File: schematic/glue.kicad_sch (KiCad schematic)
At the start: 9 parts, among them J6 Conn_02x05_Odd_Even, U9 EPM7128SLC

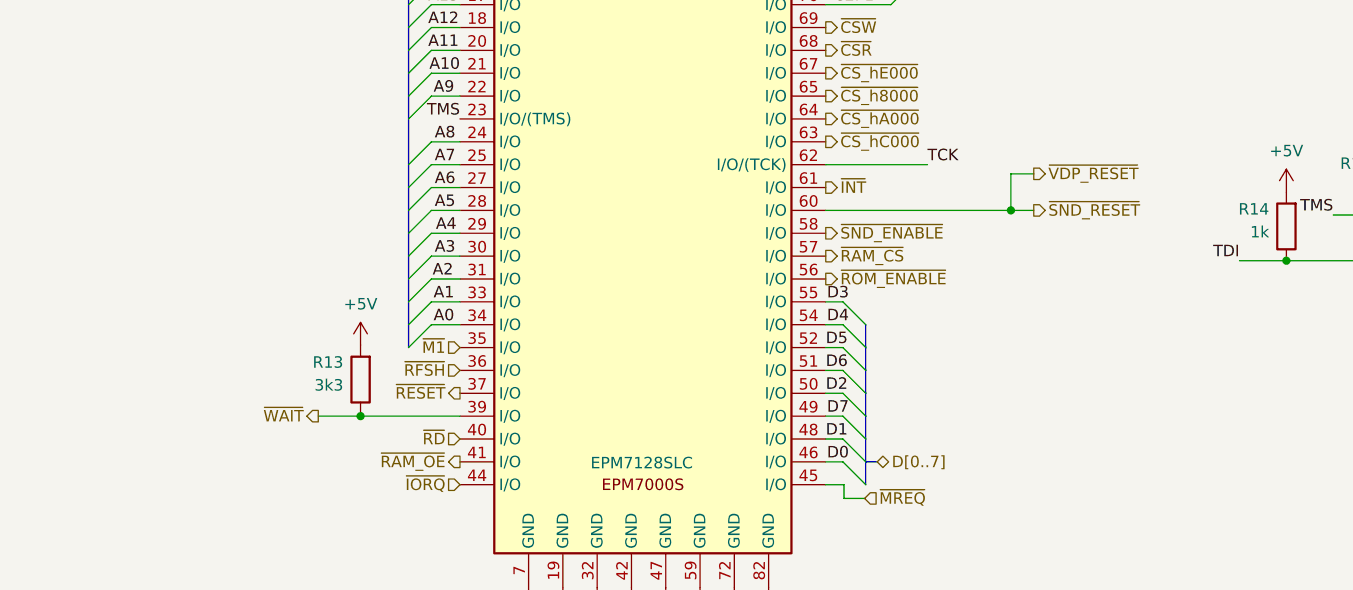
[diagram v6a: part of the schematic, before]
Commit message: complete ram mirror when banks not enabled.
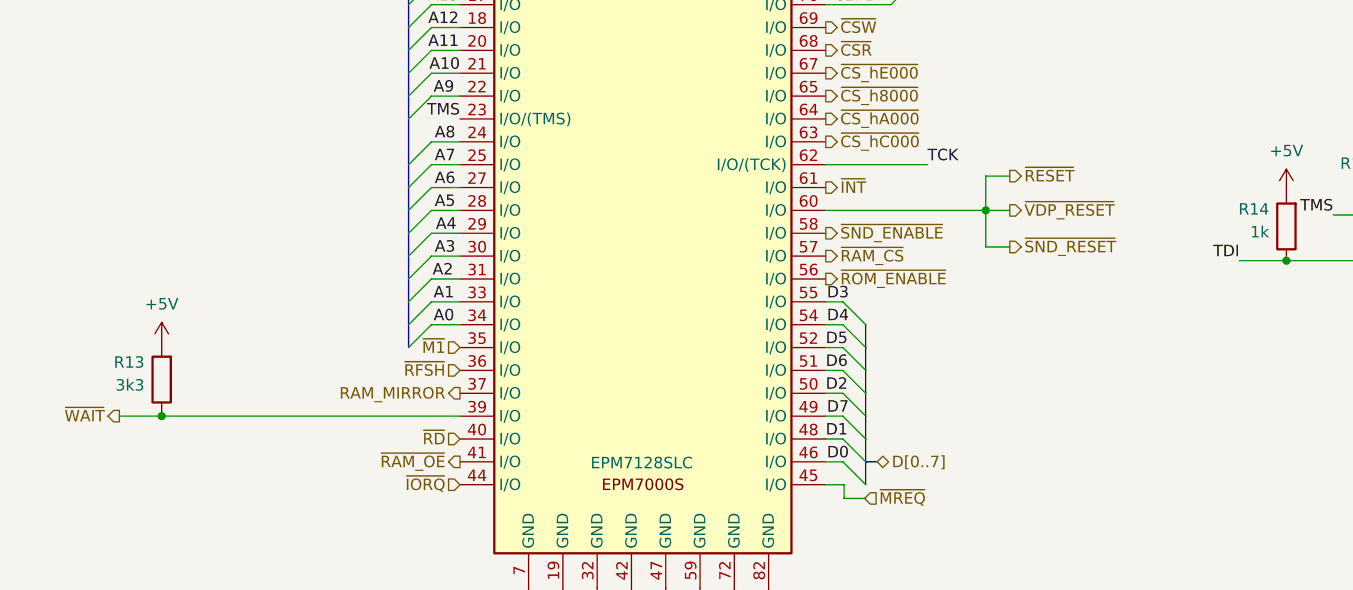
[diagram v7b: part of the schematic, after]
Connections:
- net ~{SND_RESET} is gone; now on net ~{RESET}: U9.60 (I/O)
- net ~{RESET}: no longer U9.37 (I/O)
- new net RAM_MIRROR: U9.37 (I/O)
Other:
- moved on the sheet: R13
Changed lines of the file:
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@@
   (junction (at 184.531 114.3) (diameter 0) (color 0 0 0 0)
   )
-  (junction (at 70.358 136.652) (diameter 0) (color 0 0 0 0)
+  (junction (at 48.26 136.652) (diameter 0) (color 0 0 0 0)
   )
   (junction (at 142.367 48.641) (diameter 0) (color 0 0 0 0)
@@
   (junction (at 142.367 40.386) (diameter 0) (color 0 0 0 0)
   )
-  (junction (at 142.621 113.792) (diameter 0) (color 0 0 0 0)
+  (junction (at 139.827 113.792) (diameter 0) (color 0 0 0 0)
   )
   (no_connect (at 225.298 114.3))
@@
     (stroke (width 0) (type default))
   )
-  (wire (pts (xy 145.161 113.792) (xy 142.621 113.792))
+  (wire (pts (xy 142.494 113.792) (xy 139.827 113.792))
     (stroke (width 0) (type default))
   )
@@
     (stroke (width 0) (type default))
   )
-  (wire (pts (xy 142.494 113.792) (xy 122.047 113.792))
-    (stroke (width 0) (type default))
-  )
   (bus (pts (xy 69.596 62.865) (xy 71.12 62.865))
     (stroke (width 0) (type default))
@@
     (stroke (width 0) (type default))
   )
-  (wire (pts (xy 70.358 136.652) (xy 70.358 136.398))
+  (wire (pts (xy 48.26 136.652) (xy 48.26 136.398))
     (stroke (width 0) (type default))
   )
@@
     (stroke (width 0) (type default))
   )
-  (wire (pts (xy 142.621 113.792) (xy 142.621 113.919))
-    (stroke (width 0) (type default))
-  )
   (bus (pts (xy 75.692 111.252) (xy 75.692 113.792))
     (stroke (width 0) (type default))
@@
     (stroke (width 0) (type default))
   )
-  (wire (pts (xy 145.161 109.728) (xy 142.621 109.728))
-    (stroke (width 0) (type default))
-  )
   (wire (pts (xy 78.232 123.952) (xy 81.407 123.952))
     (stroke (width 0) (type default))
@@
     (stroke (width 0) (type default))
   )
+  (wire (pts (xy 139.827 117.856) (xy 142.494 117.856))
+    (stroke (width 0) (type default))
+  )
   (bus (pts (xy 75.692 126.492) (xy 75.692 129.032))
     (stroke (width 0) (type default))
@@
     (stroke (width 0) (type default))
   )
-  (wire (pts (xy 65.659 136.652) (xy 70.358 136.652))
+  (wire (pts (xy 43.561 136.652) (xy 48.26 136.652))
     (stroke (width 0) (type default))
   )
@@
     (stroke (width 0) (type default))
   )
+  (wire (pts (xy 142.494 109.982) (xy 139.827 109.982))
+    (stroke (width 0) (type default))
+  )
   (wire (pts (xy 122.047 80.772) (xy 129.286 80.772))
     (stroke (width 0) (type default))
@@
     (stroke (width 0) (type default))
   )
-  (wire (pts (xy 142.494 113.919) (xy 142.494 113.792))
-    (stroke (width 0) (type default))
-  )
   (wire (pts (xy 122.047 83.312) (xy 129.286 83.312))
     (stroke (width 0) (type default))
@@
     (stroke (width 0) (type default))
   )
-  (wire (pts (xy 70.358 136.652) (xy 81.407 136.652))
+  (wire (pts (xy 48.26 136.652) (xy 81.407 136.652))
     (stroke (width 0) (type default))
   )
@@
     (stroke (width 0) (type default))
   )
+  (wire (pts (xy 139.827 113.792) (xy 139.827 117.856))
+    (stroke (width 0) (type default))
+  )
   (bus (pts (xy 75.692 118.872) (xy 75.692 121.412))
     (stroke (width 0) (type default))
@@
     (stroke (width 0) (type default))
   )
+  (wire (pts (xy 139.827 113.792) (xy 139.827 109.982))
+    (stroke (width 0) (type default))
+  )
   (wire (pts (xy 73.66 65.532) (xy 81.407 65.532))
     (stroke (width 0) (type default))
@@
     (stroke (width 0) (type default))
   )
+  (wire (pts (xy 122.047 113.792) (xy 139.827 113.792))
+    (stroke (width 0) (type default))
+  )
   (wire (pts (xy 81.407 90.932) (xy 78.232 90.932))
     (stroke (width 0) (type default))
@@
     (stroke (width 0) (type default))
   )
-  (wire (pts (xy 142.621 109.728) (xy 142.621 113.792))
-    (stroke (width 0) (type default))
-  )
-  (wire (pts (xy 142.621 113.919) (xy 142.494 113.919))
-    (stroke (width 0) (type default))
-  )
   (bus (pts (xy 131.826 83.312) (xy 131.826 86.36))
     (stroke (width 0) (type default))
@@
     (effects (font (size 1.27 1.27)) (justify left))
   )
+  (hierarchical_label "RAM_MIRROR" (shape output) (at 81.407 134.112 180) (fields_autoplaced)
+    (effects (font (size 1.27 1.27)) (justify right))
+  )
   (hierarchical_label "~{CSR}" (shape output) (at 122.047 96.012 0) (fields_autoplaced)
     (effects (font (size 1.27 1.27)) (justify left))
@@
     (effects (font (size 1.27 1.27)) (justify right))
   )
-  (hierarchical_label "~{WAIT}" (shape output) (at 65.659 136.652 180) (fields_autoplaced)
+  (hierarchical_label "~{WAIT}" (shape output) (at 43.561 136.652 180) (fields_autoplaced)
     (effects (font (size 1.27 1.27)) (justify right))
   )
@@
     (effects (font (size 1.27 1.27)) (justify left))
   )
-  (hierarchical_label "~{SND_RESET}" (shape output) (at 145.161 113.792 0) (fields_autoplaced)
-    (effects (font (size 1.27 1.27)) (justify left))
-  )
-  (hierarchical_label "~{VDP_RESET}" (shape output) (at 145.161 109.728 0) (fields_autoplaced)
-    (effects (font (size 1.27 1.27)) (justify left))
-  )
-  (hierarchical_label "~{RESET}" (shape output) (at 81.407 134.112 180) (fields_autoplaced)
-    (effects (font (size 1.27 1.27)) (justify right))
+  (hierarchical_label "~{SND_RESET}" (shape output) (at 142.494 117.856 0) (fields_autoplaced)
+    (effects (font (size 1.27 1.27)) (justify left))
+  )
+  (hierarchical_label "~{VDP_RESET}" (shape output) (at 142.494 113.792 0) (fields_autoplaced)
+    (effects (font (size 1.27 1.27)) (justify left))
+  )
+  (hierarchical_label "~{RESET}" (shape output) (at 142.494 109.982 0) (fields_autoplaced)
+    (effects (font (size 1.27 1.27)) (justify left))
   )
   (hierarchical_label "~{WR}" (shape input) (at 122.047 62.992 0) (fields_autoplaced)
@@
     )
   )
-  (symbol (lib_id "Device:R") (at 70.358 132.588 180) (unit 1)
+  (symbol (lib_id "Device:R") (at 48.26 132.588 180) (unit 1)
     (in_bom yes) (on_board yes) (dnp no)
-    (property "Reference" "R13" (at 68.453 130.683 0)
+    (property "Reference" "R13" (at 46.355 130.683 0)
       (effects (font (size 1.27 1.27)) (justify left))
     )
-    (property "Value" "3k3" (at 68.453 133.223 0)
+    (property "Value" "3k3" (at 46.355 133.223 0)
       (effects (font (size 1.27 1.27)) (justify left))
     )
-    (property "Footprint" "Resistor_SMD:R_0805_2012Metric" (at 72.136 132.588 90)
-      (effects (font (size 1.27 1.27)) hide)
-    )
-    (property "Datasheet" "~" (at 70.358 132.588 0)
+    (property "Footprint" "Resistor_SMD:R_0805_2012Metric" (at 50.038 132.588 90)
+      (effects (font (size 1.27 1.27)) hide)
+    )
+    (property "Datasheet" "~" (at 48.26 132.588 0)
       (effects (font (size 1.27 1.27)) hide)
     )
@@
     )
   )
-  (symbol (lib_id "power:+5V") (at 70.358 128.778 0) (unit 1)
+  (symbol (lib_id "power:+5V") (at 48.26 128.778 0) (unit 1)
     (in_bom yes) (on_board yes) (dnp no) (fields_autoplaced)
-    (property "Reference" "#PWR052" (at 70.358 132.588 0)
-      (effects (font (size 1.27 1.27)) hide)
-    )
-    (property "Value" "+5V" (at 70.358 124.206 0)
+    (property "Reference" "#PWR052" (at 48.26 132.588 0)
+      (effects (font (size 1.27 1.27)) hide)
+    )
+    (property "Value" "+5V" (at 48.26 124.206 0)
       (effects (font (size 1.27 1.27)))
     )
-    (property "Footprint" "" (at 70.358 128.778 0)
-      (effects (font (size 1.27 1.27)) hide)
-    )
-    (property "Datasheet" "" (at 70.358 128.778 0)
-      (effects (font (size 1.27 1.27)) hide)
-    )
+    (property "Footprint" "" (at 48.26 128.778 0)
+      (effects (font (size 1.27 1.27)) hide)
+    )
+    (property "Datasheet" "" (at 48.26 128.778 0)
+      (effects (font (size 1.27 1.27)) hide)
+    )
